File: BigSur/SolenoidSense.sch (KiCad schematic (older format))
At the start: 33 parts, among them U10 MCP6L02T-E_MS, U11 74LVC1G00W5-7, U12 ACS70331EESATR-2P5U3, U5 ACS70331EESATR-2P5U3, U6 ACS70331EESATR-2P5U3, U7 ACS70331EESATR-2P5U3, U8 ACS70331EESATR-2P5U3, U9 ACS70331EESATR-2P5U3

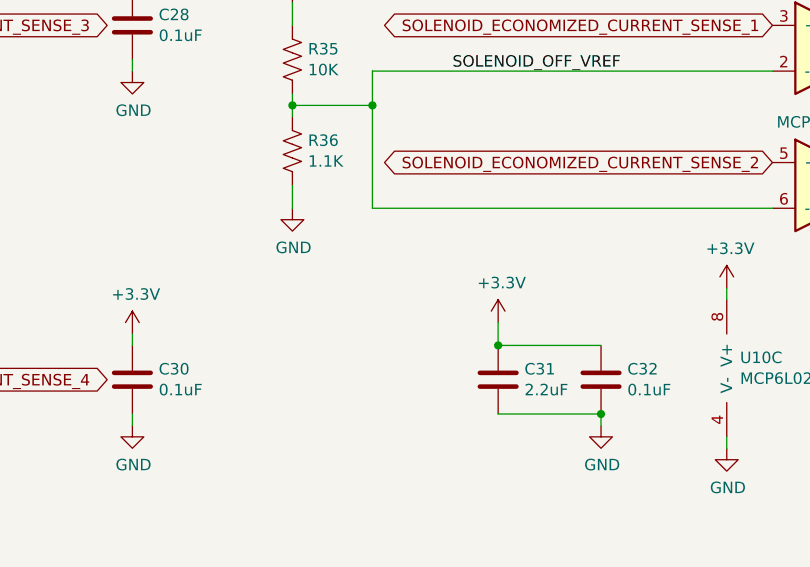
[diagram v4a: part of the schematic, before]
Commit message: Added indicator LED for braking
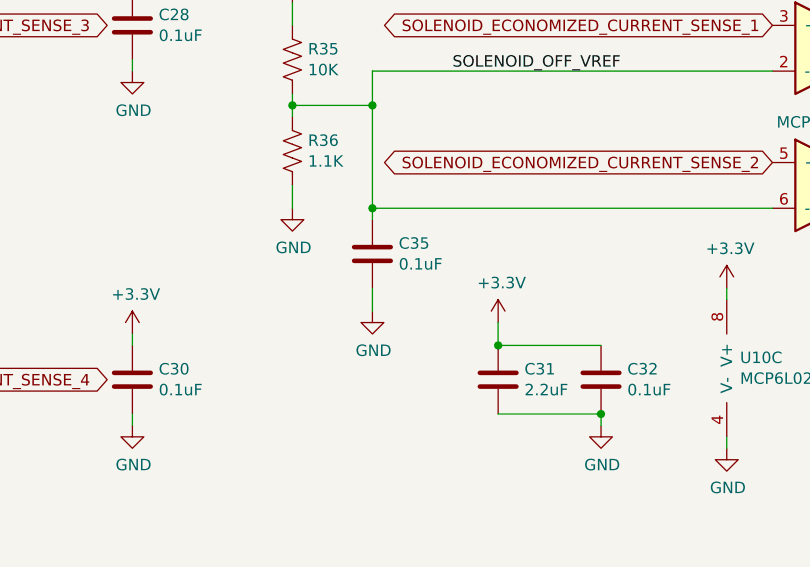
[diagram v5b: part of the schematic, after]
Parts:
- added C35: 0.1uF, Capacitor_SMD:C_0603_1608Metric_Pad1.05x0.95mm_HandSolder, symbol Device:C
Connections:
- net GND: now also C35.2
- net SOLENOID_OFF_VREF: now also C35.1
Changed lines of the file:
@@
 Text Label 6200 4550 0    50   ~ 0
 SOLENOID_OFF_VREF
-Wire Wire Line
-	5500 4700 5500 4750
-Connection ~ 5500 4700
-$Comp
-L power:GND #PWR0103
-U 1 1 5DAB40A2
-P 5500 5150
-F 0 "#PWR0103" H 5500 4900 50  0001 C CNN
-F 1 "GND" H 5505 4977 50  0000 C CNN
-F 2 "" H 5500 5150 50  0001 C CNN
-F 3 "" H 5500 5150 50  0001 C CNN
-	1    5500 5150
-	1    0    0    -1
-$EndComp
-Wire Wire Line
-	5500 5050 5500 5150
-Wire Wire Line
-	5500 4650 5500 4700
-Wire Wire Line
-	5500 4250 5500 4350
-$Comp
-L power:+3.3V #PWR099
-U 1 1 5DAAE3B5
-P 5500 4250
-F 0 "#PWR099" H 5500 4100 50  0001 C CNN
-F 1 "+3.3V" H 5515 4423 50  0000 C CNN
-F 2 "" H 5500 4250 50  0001 C CNN
-F 3 "" H 5500 4250 50  0001 C CNN
-	1    5500 4250
-	1    0    0    -1
-$EndComp
-$Comp
-L Device:R_US R36
-U 1 1 5DAADB59
-P 5500 4900
-F 0 "R36" H 5568 4946 50  0000 L CNN
-F 1 "1.1K" H 5568 4855 50  0000 L CNN
-F 2 "Resistor_SMD:R_0603_1608Metric_Pad1.05x0.95mm_HandSolder" V 5540 4890 50  0001 C CNN
-F 3 "https://www.seielect.com/catalog/sei-rmcf_rmcp.pdf" H 5500 4900 50  0001 C CNN
-F 4 "https://www.digikey.ca/product-detail/en/stackpole-electronics-inc/RMCF0603FT1K10/RMCF0603FT1K10CT-ND/2417966" H 5500 4900 50  0001 C CNN "Digikey"
-F 5 "RMCF0603FT1K10" H 5500 4900 50  0001 C CNN "Part Number"
-	1    5500 4900
-	1    0    0    -1
-$EndComp
-$Comp
-L Device:R_US R35
-U 1 1 5DAAC33E
-P 5500 4500
-F 0 "R35" H 5568 4546 50  0000 L CNN
-F 1 "10K" H 5568 4455 50  0000 L CNN
-F 2 "Resistor_SMD:R_0603_1608Metric_Pad1.05x0.95mm_HandSolder" V 5540 4490 50  0001 C CNN
-F 3 "https://www.seielect.com/catalog/sei-rncp.pdf" H 5500 4500 50  0001 C CNN
-F 4 "https://www.digikey.ca/product-detail/en/stackpole-electronics-inc/RNCP0603FTD10K0/RNCP0603FTD10K0CT-ND/2240478" H 5500 4500 50  0001 C CNN "Part Number"
-F 5 "RNCP0603FTD10K0" H 5500 4500 50  0001 C CNN "Digikey"
-	1    5500 4500
-	1    0    0    -1
-$EndComp
 Connection ~ 5850 4700
 Wire Wire Line
@@
 Wire Wire Line
 	5850 4700 5850 4550
-Wire Wire Line
-	5500 4700 5850 4700
 Text GLabel 7600 4350 0    50   BiDi ~ 0
 SOLENOID_ECONOMIZED_CURRENT_SENSE_1
@@
 Wire Wire Line
 	9150 3850 9150 3950
+Wire Wire Line
+	5500 4700 5850 4700
+$Comp
+L Device:R_US R35
+U 1 1 5DAAC33E
+P 5500 4500
+F 0 "R35" H 5568 4546 50  0000 L CNN
+F 1 "10K" H 5568 4455 50  0000 L CNN
+F 2 "Resistor_SMD:R_0603_1608Metric_Pad1.05x0.95mm_HandSolder" V 5540 4490 50  0001 C CNN
+F 3 "https://www.seielect.com/catalog/sei-rncp.pdf" H 5500 4500 50  0001 C CNN
+F 4 "https://www.digikey.ca/product-detail/en/stackpole-electronics-inc/RNCP0603FTD10K0/RNCP0603FTD10K0CT-ND/2240478" H 5500 4500 50  0001 C CNN "Part Number"
+F 5 "RNCP0603FTD10K0" H 5500 4500 50  0001 C CNN "Digikey"
+	1    5500 4500
+	1    0    0    -1
+$EndComp
+$Comp
+L Device:R_US R36
+U 1 1 5DAADB59
+P 5500 4900
+F 0 "R36" H 5568 4946 50  0000 L CNN
+F 1 "1.1K" H 5568 4855 50  0000 L CNN
+F 2 "Resistor_SMD:R_0603_1608Metric_Pad1.05x0.95mm_HandSolder" V 5540 4890 50  0001 C CNN
+F 3 "https://www.seielect.com/catalog/sei-rmcf_rmcp.pdf" H 5500 4900 50  0001 C CNN
+F 4 "https://www.digikey.ca/product-detail/en/stackpole-electronics-inc/RMCF0603FT1K10/RMCF0603FT1K10CT-ND/2417966" H 5500 4900 50  0001 C CNN "Digikey"
+F 5 "RMCF0603FT1K10" H 5500 4900 50  0001 C CNN "Part Number"
+	1    5500 4900
+	1    0    0    -1
+$EndComp
+$Comp
+L power:+3.3V #PWR099
+U 1 1 5DAAE3B5
+P 5500 4250
+F 0 "#PWR099" H 5500 4100 50  0001 C CNN
+F 1 "+3.3V" H 5515 4423 50  0000 C CNN
+F 2 "" H 5500 4250 50  0001 C CNN
+F 3 "" H 5500 4250 50  0001 C CNN
+	1    5500 4250
+	1    0    0    -1
+$EndComp
+Wire Wire Line
+	5500 4250 5500 4350
+Wire Wire Line
+	5500 4650 5500 4700
+Wire Wire Line
+	5500 5050 5500 5150
+$Comp
+L power:GND #PWR0103
+U 1 1 5DAB40A2
+P 5500 5150
+F 0 "#PWR0103" H 5500 4900 50  0001 C CNN
+F 1 "GND" H 5505 4977 50  0000 C CNN
+F 2 "" H 5500 5150 50  0001 C CNN
+F 3 "" H 5500 5150 50  0001 C CNN
+	1    5500 5150
+	1    0    0    -1
+$EndComp
+Connection ~ 5500 4700
+Wire Wire Line
+	5500 4700 5500 4750
+$Comp
+L Device:C C?
+U 1 1 5DAC261B
+P 5850 5350
+AR Path="/5D6EB2B2/5DAC261B" Ref="C?"  Part="1"
+AR Path="/5D71C3EA/5DAC261B" Ref="C?"  Part="1"
+AR Path="/5D765C4F/5DAC261B" Ref="C35"  Part="1"
+F 0 "C35" H 5965 5396 50  0000 L CNN
+F 1 "0.1uF" H 5965 5305 50  0000 L CNN
+F 2 "Capacitor_SMD:C_0603_1608Metric_Pad1.05x0.95mm_HandSolder" H 5850 5350 50  0001 C CNN
+F 3 "http://www.samsungsem.com/kr/support/product-search/mlcc/__icsFiles/afieldfile/2019/06/18/CL10B104KB8NNNC-19.pdf" H 5850 5350 50  0001 C CNN
+F 4 "CL10B104KB8NNNC" H 5850 5350 50  0001 C CNN "Part Number"
+F 5 "https://www.digikey.ca/product-detail/en/samsung-electro-mechanics/CL10B104KB8NNNC/1276-1000-1-ND/3889086" H 5850 5350 50  0001 C CNN "Digikey"
+	1    5850 5350
+	1    0    0    -1
+$EndComp
+Wire Wire Line
+	5850 5150 5850 5200
+Connection ~ 5850 5150
+Wire Wire Line
+	5850 5500 5850 5600
+$Comp
+L power:GND #PWR0117
+U 1 1 5DACFFE3
+P 5850 5600
+F 0 "#PWR0117" H 5850 5350 50  0001 C CNN
+F 1 "GND" H 5855 5427 50  0000 C CNN
+F 2 "" H 5850 5600 50  0001 C CNN
+F 3 "" H 5850 5600 50  0001 C CNN
+	1    5850 5600
+	1    0    0    -1
+$EndComp
 $EndSCHEMATC

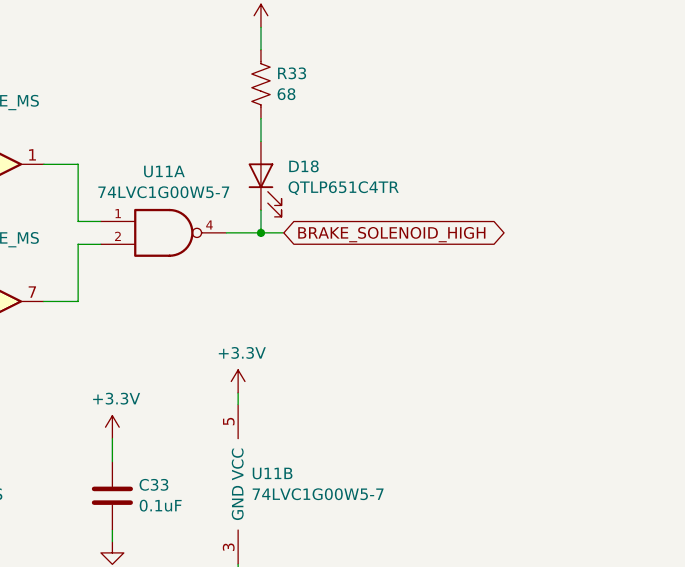
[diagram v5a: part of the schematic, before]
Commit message: Cleaned up comments. (sorry for the electrical alerts spam bys)
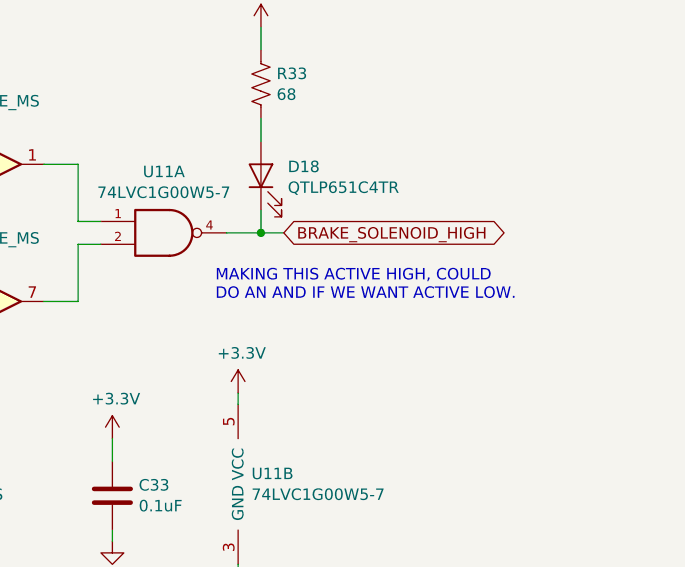
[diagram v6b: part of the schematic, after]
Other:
- note added: "MAKING THIS ACTIVE HIGH, COULD\nDO AN AND IF WE WANT ACTIVE LOW."
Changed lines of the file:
@@
 	1    0    0    -1
 $EndComp
+Text Notes 8950 5050 0    50   ~ 0
+MAKING THIS ACTIVE HIGH, COULD\nDO AN AND IF WE WANT ACTIVE LOW.
 $EndSCHEMATC

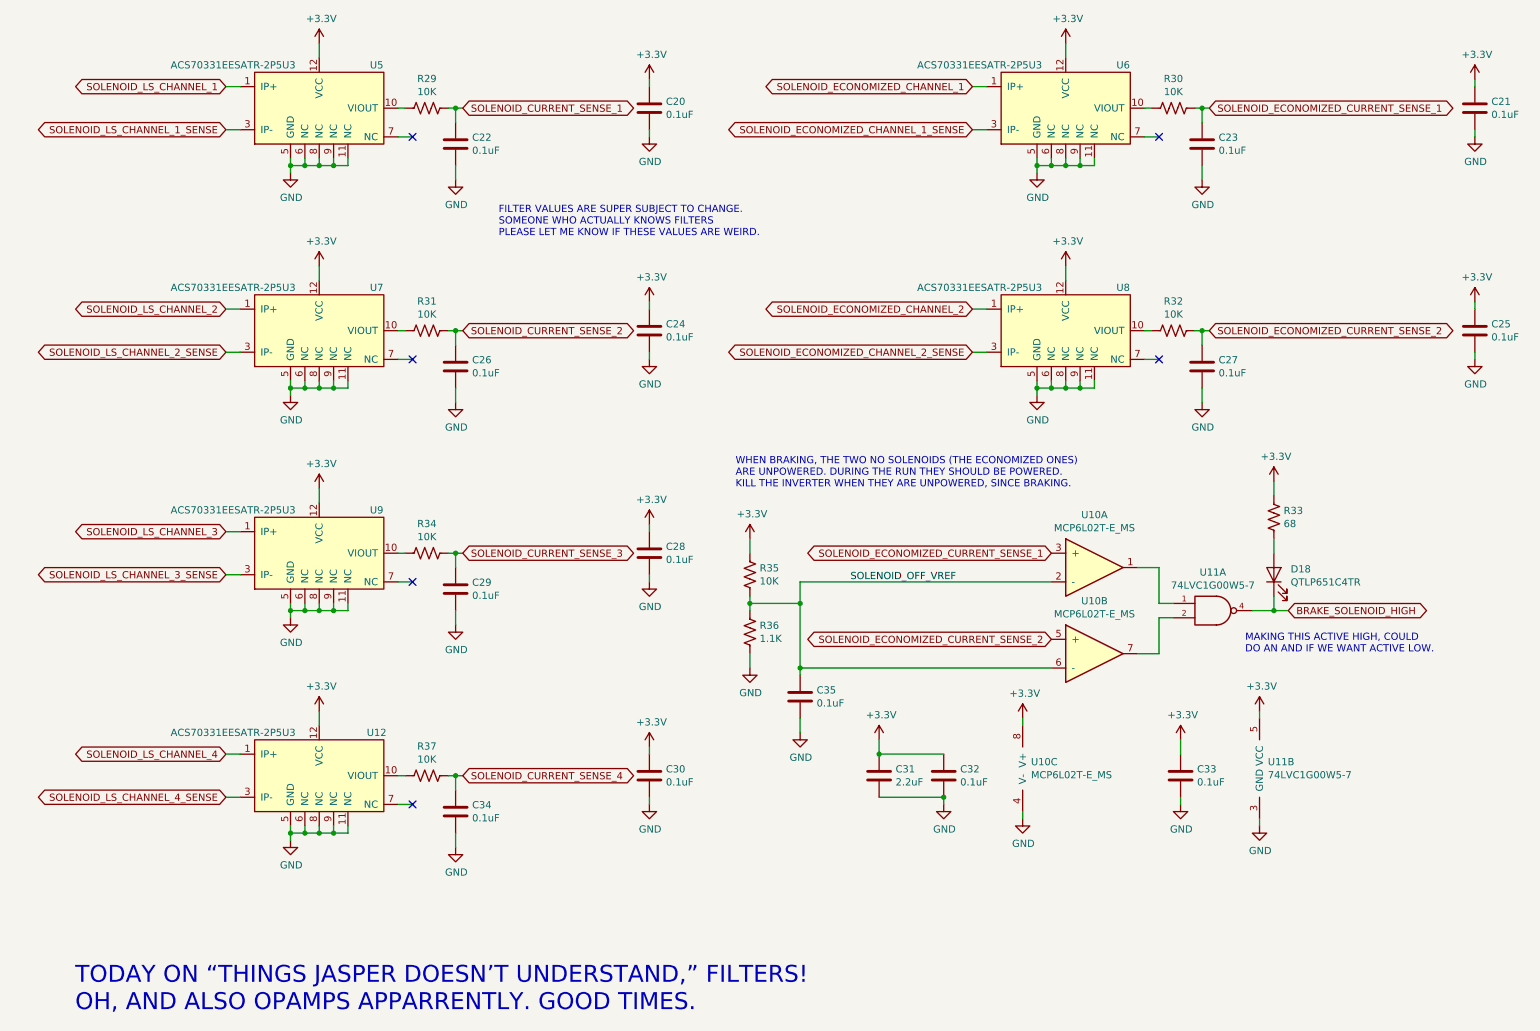
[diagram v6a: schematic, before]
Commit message: Fixed current sense, added GP relay LEDs
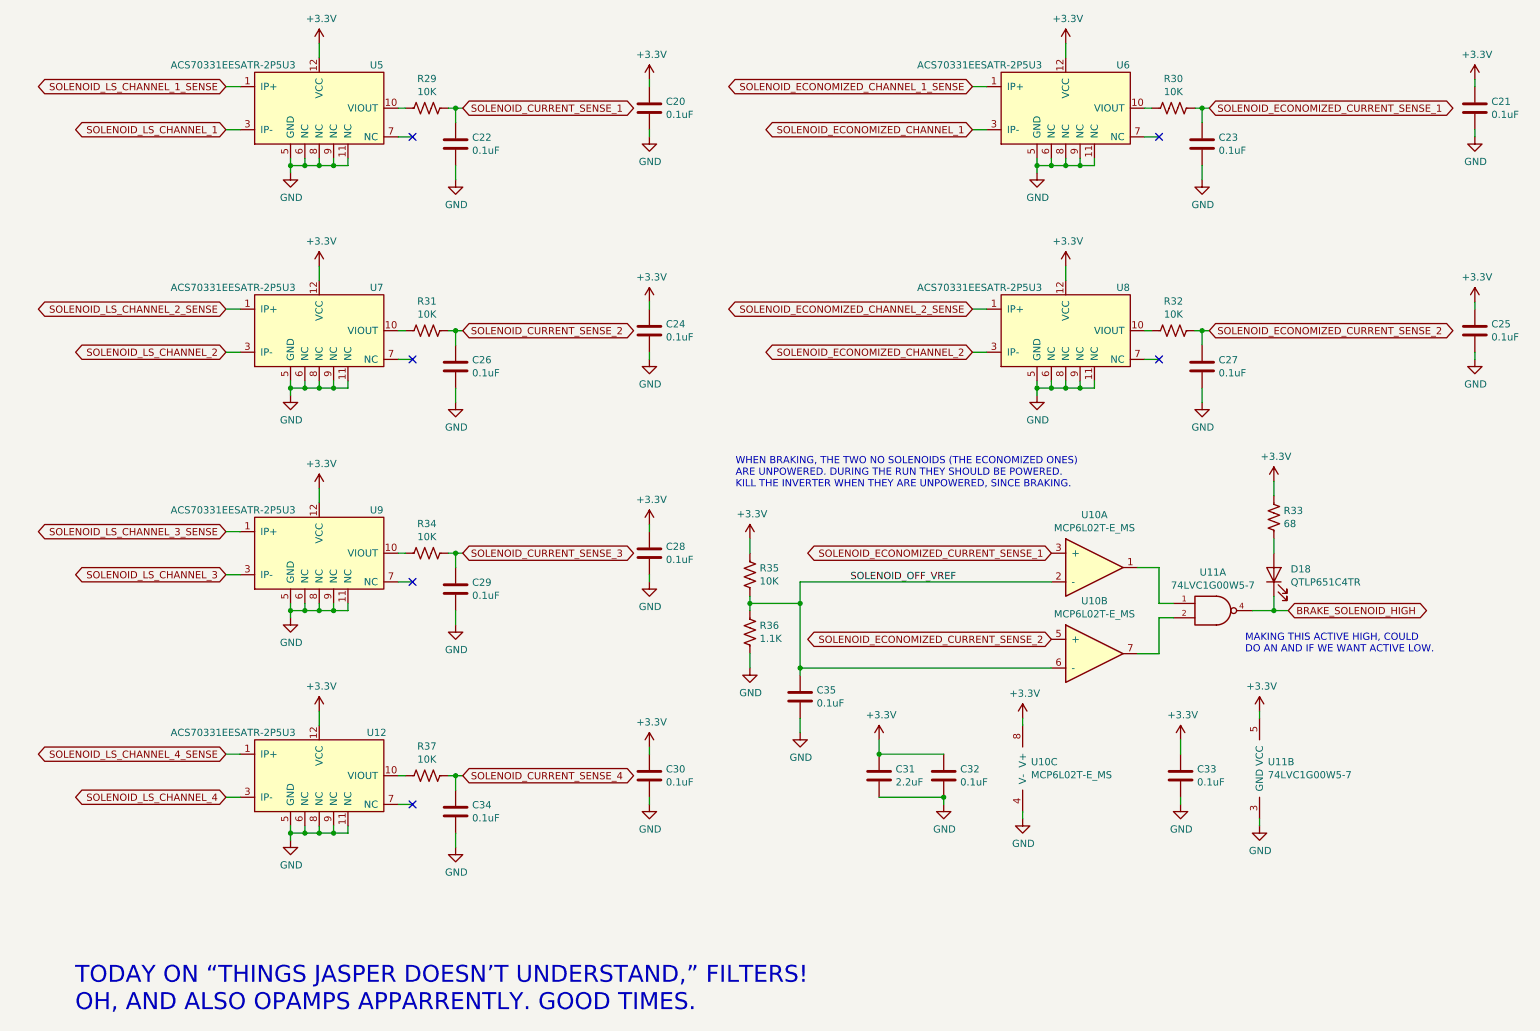
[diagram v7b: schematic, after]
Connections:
- net SOLENOID_ECONOMIZED_CHANNEL_1: now also U6.3 (IP-); no longer U6.1 (IP+)
- net SOLENOID_ECONOMIZED_CHANNEL_1_SENSE: now also U6.1 (IP+); no longer U6.3 (IP-)
- net SOLENOID_ECONOMIZED_CHANNEL_2: now also U8.3 (IP-); no longer U8.1 (IP+)
- net SOLENOID_ECONOMIZED_CHANNEL_2_SENSE: now also U8.1 (IP+); no longer U8.3 (IP-)
- net SOLENOID_LS_CHANNEL_1: now also U5.3 (IP-); no longer U5.1 (IP+)
- net SOLENOID_LS_CHANNEL_1_SENSE: now also U5.1 (IP+); no longer U5.3 (IP-)
- net SOLENOID_LS_CHANNEL_2: now also U7.3 (IP-); no longer U7.1 (IP+)
- net SOLENOID_LS_CHANNEL_2_SENSE: now also U7.1 (IP+); no longer U7.3 (IP-)
- net SOLENOID_LS_CHANNEL_3: now also U9.3 (IP-); no longer U9.1 (IP+)
- net SOLENOID_LS_CHANNEL_3_SENSE: now also U9.1 (IP+); no longer U9.3 (IP-)
- net SOLENOID_LS_CHANNEL_4: now also U12.3 (IP-); no longer U12.1 (IP+)
- net SOLENOID_LS_CHANNEL_4_SENSE: now also U12.1 (IP+); no longer U12.3 (IP-)
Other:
- note removed: "FILTER VALUES ARE SUPER SUBJECT TO CHANGE.\nSOMEONE WHO ACTUALLY KNOWS FILTERS\nPLEASE LET ME KNOW IF THESE VALUES ARE WEIRD."
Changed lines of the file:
@@
 Wire Wire Line
 	3100 1250 3050 1250
+Text GLabel 1850 1100 0    50   BiDi ~ 0
+SOLENOID_LS_CHANNEL_1_SENSE
+Wire Wire Line
+	1850 1100 1950 1100
 Text GLabel 1850 1400 0    50   BiDi ~ 0
-SOLENOID_LS_CHANNEL_1_SENSE
-Wire Wire Line
-	1850 1100 1950 1100
-Text GLabel 1850 1100 0    50   BiDi ~ 0
 SOLENOID_LS_CHANNEL_1
 Text GLabel 8700 1250 2    50   BiDi ~ 0
 SOLENOID_ECONOMIZED_CURRENT_SENSE_1
+Text GLabel 7050 1100 0    50   BiDi ~ 0
+SOLENOID_ECONOMIZED_CHANNEL_1_SENSE
 Text GLabel 7050 1400 0    50   BiDi ~ 0
-SOLENOID_ECONOMIZED_CHANNEL_1_SENSE
-Text GLabel 7050 1100 0    50   BiDi ~ 0
 SOLENOID_ECONOMIZED_CHANNEL_1
 Wire Wire Line
@@
 Text Notes 800  7550 0    118  ~ 0
 TODAY ON “THINGS JASPER DOESN’T UNDERSTAND,” FILTERS!\nOH, AND ALSO OPAMPS APPARRENTLY. GOOD TIMES.
-Text Notes 3750 2150 0    50   ~ 0
-FILTER VALUES ARE SUPER SUBJECT TO CHANGE.\nSOMEONE WHO ACTUALLY KNOWS FILTERS\nPLEASE LET ME KNOW IF THESE VALUES ARE WEIRD.
 Text Notes 5400 3900 0    50   ~ 0
 WHEN BRAKING, THE TWO NO SOLENOIDS (THE ECONOMIZED ONES)\nARE UNPOWERED. DURING THE RUN THEY SHOULD BE POWERED.\nKILL THE INVERTER WHEN THEY ARE UNPOWERED, SINCE BRAKING.
@@
 Wire Wire Line
 	3100 2800 3050 2800
+Text GLabel 1850 2650 0    50   BiDi ~ 0
+SOLENOID_LS_CHANNEL_2_SENSE
+Wire Wire Line
+	1850 2650 1950 2650
 Text GLabel 1850 2950 0    50   BiDi ~ 0
-SOLENOID_LS_CHANNEL_2_SENSE
-Wire Wire Line
-	1850 2650 1950 2650
-Text GLabel 1850 2650 0    50   BiDi ~ 0
 SOLENOID_LS_CHANNEL_2
 Wire Wire Line
@@
 Wire Wire Line
 	3100 4350 3050 4350
+Text GLabel 1850 4200 0    50   BiDi ~ 0
+SOLENOID_LS_CHANNEL_3_SENSE
+Wire Wire Line
+	1850 4200 1950 4200
 Text GLabel 1850 4500 0    50   BiDi ~ 0
-SOLENOID_LS_CHANNEL_3_SENSE
-Wire Wire Line
-	1850 4200 1950 4200
-Text GLabel 1850 4200 0    50   BiDi ~ 0
 SOLENOID_LS_CHANNEL_3
 Wire Wire Line
@@
 Wire Wire Line
 	3100 5900 3050 5900
+Text GLabel 1850 5750 0    50   BiDi ~ 0
+SOLENOID_LS_CHANNEL_4_SENSE
+Wire Wire Line
+	1850 5750 1950 5750
 Text GLabel 1850 6050 0    50   BiDi ~ 0
-SOLENOID_LS_CHANNEL_4_SENSE
-Wire Wire Line
-	1850 5750 1950 5750
-Text GLabel 1850 5750 0    50   BiDi ~ 0
 SOLENOID_LS_CHANNEL_4
 Wire Wire Line
@@
 Text GLabel 8700 2800 2    50   BiDi ~ 0
 SOLENOID_ECONOMIZED_CURRENT_SENSE_2
+Text GLabel 7050 2650 0    50   BiDi ~ 0
+SOLENOID_ECONOMIZED_CHANNEL_2_SENSE
 Text GLabel 7050 2950 0    50   BiDi ~ 0
-SOLENOID_ECONOMIZED_CHANNEL_2_SENSE
-Text GLabel 7050 2650 0    50   BiDi ~ 0
 SOLENOID_ECONOMIZED_CHANNEL_2
 $Comp

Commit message: Cleaned up schematics
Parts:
- renumbered C35 to C30, C30 to C31, C31 to C32, C32 to C33, C33 to C34, C34 to C35, D18 to D22, R29 to R33, R30 to R34, R31 to R35, R32 to R36, R33 to R37, R34 to R38, R35 to R39, R36 to R40, R37 to R41
